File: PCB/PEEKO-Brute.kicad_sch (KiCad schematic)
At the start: 55 parts, among them J1 Rasberry PI Pico, J2 Conn_02x15_Odd_Even, J3 Conn_01x02_Pin, J4 Conn_01x02_Pin

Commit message: add fab bom and centroid exports
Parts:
- D1, D10, D11, D12, D13, D14, D15, D16, D17, D18, D19, D2, D20, D21, D22, D23, D24, D25, D3, D4, D5, D6, D7, D8, D9: MPN (none) -> Nexperia BAV99,215
- J1: MPN (none) -> SC0915
- J2: MPN (none) -> SBH11-PBPC-D15-ST-BK
- J3, J4: MPN (none) -> PH1RB-02-UA
- R1, R10, R11, R12, R13, R14, R15, R16, R17, R18, R19, R2, R20, R21, R22, R23, R24, R3, R4, R5, R6, R7, R8, R9: MPN (none) -> CRGCQ0805F220R
- R25: MPN (none) -> RC0805FR-07100KL
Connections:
- net TRIGGER: no longer J2.3 (Pin_3)

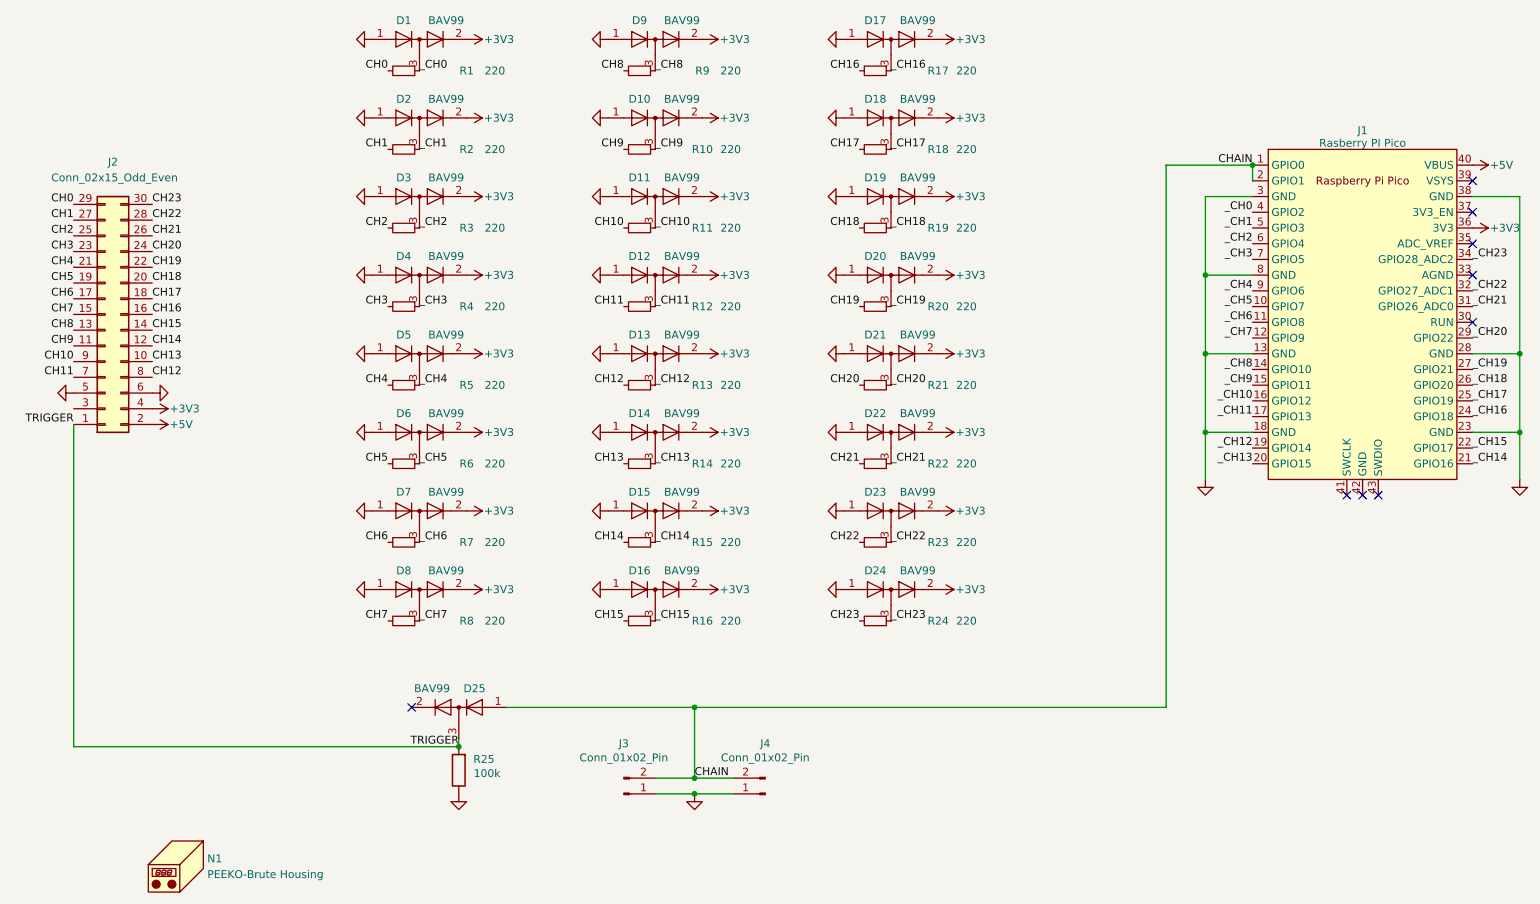
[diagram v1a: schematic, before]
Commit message: switch to schottkys on brute
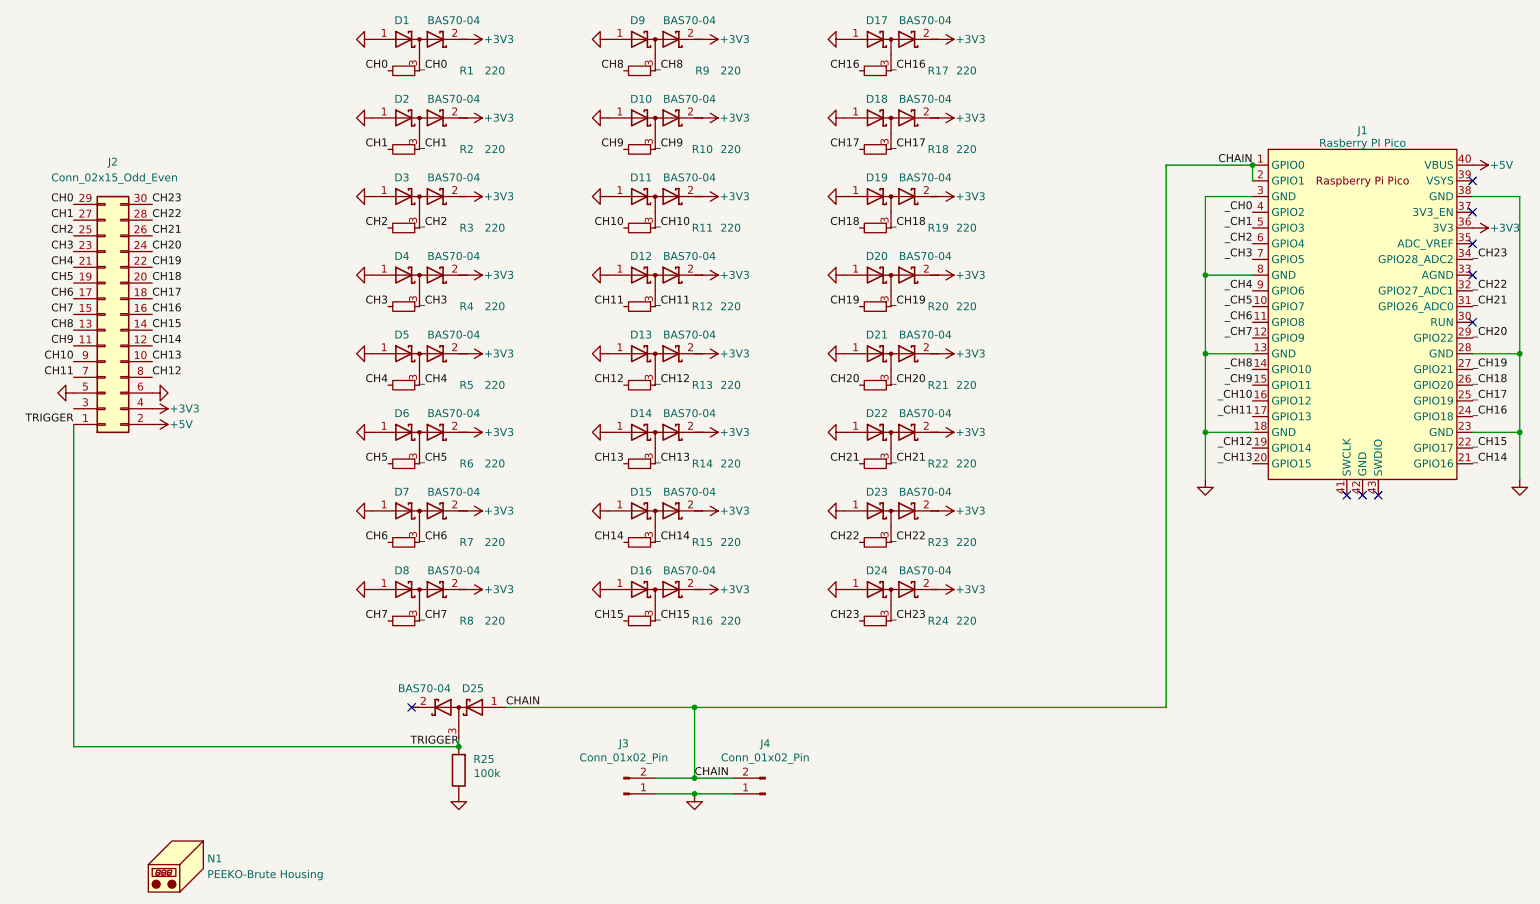
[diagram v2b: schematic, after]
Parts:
- removed D1, D10, D11, D12, D13, D14, D15, D16, D17, D18, D19, D2, D20, D21, D22, D23, D24, D25, D3, D4, D5, D6, D7, D8, D9: BAV99, 000_LOCAL:SC-59, symbol 000_LOCAL:BAV99
- added D1, D10, D11, D12, D13, D14, D15, D16, D17, D18, D19, D2, D20, D21, D22, D23, D24, D25, D3, D4, D5, D6, D7, D8, D9: BAS70-04, 000_LOCAL:SC-59, symbol 000_LOCAL:D_Schottky_Dual_Series_AKC
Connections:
- net +3V3: now also D1.2 (K), D10.2 (K), D11.2 (K), D12.2 (K), D13.2 (K), D14.2 (K), D15.2 (K), D16.2 (K), D17.2 (K), D18.2 (K), D19.2 (K), D2.2 (K), D20.2 (K), D21.2 (K), D22.2 (K), D23.2 (K), D24.2 (K), D3.2 (K), D4.2 (K), D5.2 (K), D6.2 (K), D7.2 (K), D8.2 (K), D9.2 (K)
- net CHAIN: now also D25.1 (A)
- net GND: now also D1.1 (A), D10.1 (A), D11.1 (A), D12.1 (A), D13.1 (A), D14.1 (A), D15.1 (A), D16.1 (A), D17.1 (A), D18.1 (A), D19.1 (A), D2.1 (A), D20.1 (A), D21.1 (A), D22.1 (A), D23.1 (A), D24.1 (A), D3.1 (A), D4.1 (A), D5.1 (A), D6.1 (A), D7.1 (A), D8.1 (A), D9.1 (A)
- net TRIGGER: now also D25.3 (common)
- net _CH0: now also D1.3 (common)
- net _CH1: now also D2.3 (common)
- net _CH10: now also D11.3 (common)
- net _CH11: now also D12.3 (common)
- net _CH12: now also D13.3 (common)
- net _CH13: now also D14.3 (common)
- net _CH14: now also D15.3 (common)
- net _CH15: now also D16.3 (common)
- net _CH16: now also D17.3 (common)
- net _CH17: now also D18.3 (common)
- net _CH18: now also D19.3 (common)
- net _CH19: now also D20.3 (common)
- net _CH2: now also D3.3 (common)
- net _CH20: now also D21.3 (common)
- net _CH21: now also D22.3 (common)
- net _CH22: now also D23.3 (common)
- net _CH23: now also D24.3 (common)
- net _CH3: now also D4.3 (common)
- net _CH4: now also D5.3 (common)
- net _CH5: now also D6.3 (common)
- net _CH6: now also D7.3 (common)
- net _CH7: now also D8.3 (common)
- net _CH8: now also D9.3 (common)
- net _CH9: now also D10.3 (common)

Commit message: make brute the same dimensions and port placement as regular peeko, use same housing for both
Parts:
- N1: value PEEKO-Brute Housing -> PEEKO Housing; footprint 000_LOCAL:PEEKO-Brute_housing -> 000_LOCAL:PEEKO_housing
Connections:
- net TRIGGER: now also J2.3 (Pin_3)
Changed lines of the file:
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@@
+	)
+	(junction
+		(at 33.02 113.03)
+		(diameter 0)
+		(color 0 0 0 0)
 	)
 	(junction
@@
 	(no_connect
 		(at 238.76 124.46)
+	)
+	(wire
+		(pts
+			(xy 33.02 110.49) (xy 33.02 113.03)
+		)
+		(stroke
+			(width 0)
+			(type default)
+		)
 	)
 	(wire
@@
 			)
 		)
-		(property "Value" "PEEKO-Brute Housing"
+		(property "Value" "PEEKO Housing"
 			(at 54.61 185.7374 0)
 			(effects
@@
 			)
 		)
-		(property "Footprint" "000_LOCAL:PEEKO-Brute_housing"
+		(property "Footprint" "000_LOCAL:PEEKO_housing"
 			(at 52.07 182.88 0)
 			(effects

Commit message: make both boards have same chain pinout
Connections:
- net CHAIN: now also J3.1 (Pin_1), J4.1 (Pin_1); no longer J3.2 (Pin_2), J4.2 (Pin_2)
- net GND: now also J3.2 (Pin_2), J4.2 (Pin_2); no longer J3.1 (Pin_1), J4.1 (Pin_1)
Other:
- moved on the sheet: J4
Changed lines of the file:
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@@
 	(symbol
 		(lib_id "000_LOCAL:Conn_01x02_Pin")
-		(at 144.78 172.72 180)
+		(at 144.78 170.18 0)
+		(mirror y)
 		(unit 1)
 		(exclude_from_sim no)
@@
 		(dnp no)
 		(property "Reference" "J4"
-			(at 144.78 164.592 0)
+			(at 144.78 178.308 0)
 			(effects
 				(font
@@
 		)
 		(property "Value" "Conn_01x02_Pin"
-			(at 144.78 166.878 0)
+			(at 144.78 176.022 0)
 			(effects
 				(font
@@
 		)
 		(property "Footprint" "000_LOCAL:PinHeader_1x02_P2.54mm_Horizontal"
-			(at 144.78 172.72 0)
+			(at 144.78 170.18 0)
 			(effects
 				(font
@@
 		)
 		(property "Datasheet" "~"
-			(at 144.78 172.72 0)
+			(at 144.78 170.18 0)
 			(effects
 				(font
@@
 		)
 		(property "Description" "CONN HEADER R/A 2POS 2.54MM"
-			(at 144.78 172.72 0)
+			(at 144.78 170.18 0)
 			(effects
 				(font
@@
 		)
 		(property "MPN" "PH1RB-02-UA"
-			(at 144.78 172.72 0)
+			(at 144.78 170.18 0)
 			(effects
 				(font
@@
 	(symbol
 		(lib_id "000_LOCAL:Conn_01x02_Pin")
-		(at 121.92 172.72 0)
-		(mirror x)
+		(at 121.92 170.18 0)
 		(unit 1)
 		(exclude_from_sim no)
@@
 		(dnp no)
 		(property "Reference" "J3"
-			(at 121.92 164.592 0)
+			(at 121.92 178.308 0)
 			(effects
 				(font
@@
 		)
 		(property "Value" "Conn_01x02_Pin"
-			(at 121.92 166.878 0)
+			(at 121.92 176.022 0)
 			(effects
 				(font
@@
 		)
 		(property "Footprint" "000_LOCAL:PinHeader_1x02_P2.54mm_Horizontal"
-			(at 121.92 172.72 0)
+			(at 121.92 170.18 0)
 			(effects
 				(font
@@
 		)
 		(property "Datasheet" "~"
-			(at 121.92 172.72 0)
+			(at 121.92 170.18 0)
 			(effects
 				(font
@@
 		)
 		(property "Description" "CONN HEADER R/A 2POS 2.54MM"
-			(at 121.92 172.72 0)
+			(at 121.92 170.18 0)
 			(effects
 				(font
@@
 		)
 		(property "MPN" "PH1RB-02-UA"
-			(at 121.92 172.72 0)
-			(effects
-				(font
+			(at 121.92 170.18 0)
+			(effects
+				(font

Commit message: boms
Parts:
- D1, D10, D11, D12, D13, D14, D15, D16, D17, D18, D19, D2, D20, D21, D22, D23, D24, D25, D3, D4, D5, D6, D7, D8, D9: MPN (none) -> BAS70-04
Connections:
- net CHAIN: now also D25.2 (K); no longer D25.1 (A)
